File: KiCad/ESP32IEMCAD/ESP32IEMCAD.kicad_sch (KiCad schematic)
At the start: 49 parts, among them J1 AudioJack3, J2 USB_C_Receptacle_PowerOnly_6P, J3 BOOT, J4 UART, J5 JTAG, SW1 SW_Nidec_CAS-120A1, SW2 Interpolation Mode, SW3 Hardware Mute, U1 PCM5102, U2 ESP32-WROOM-32U, U3 MAX97220AETE_T

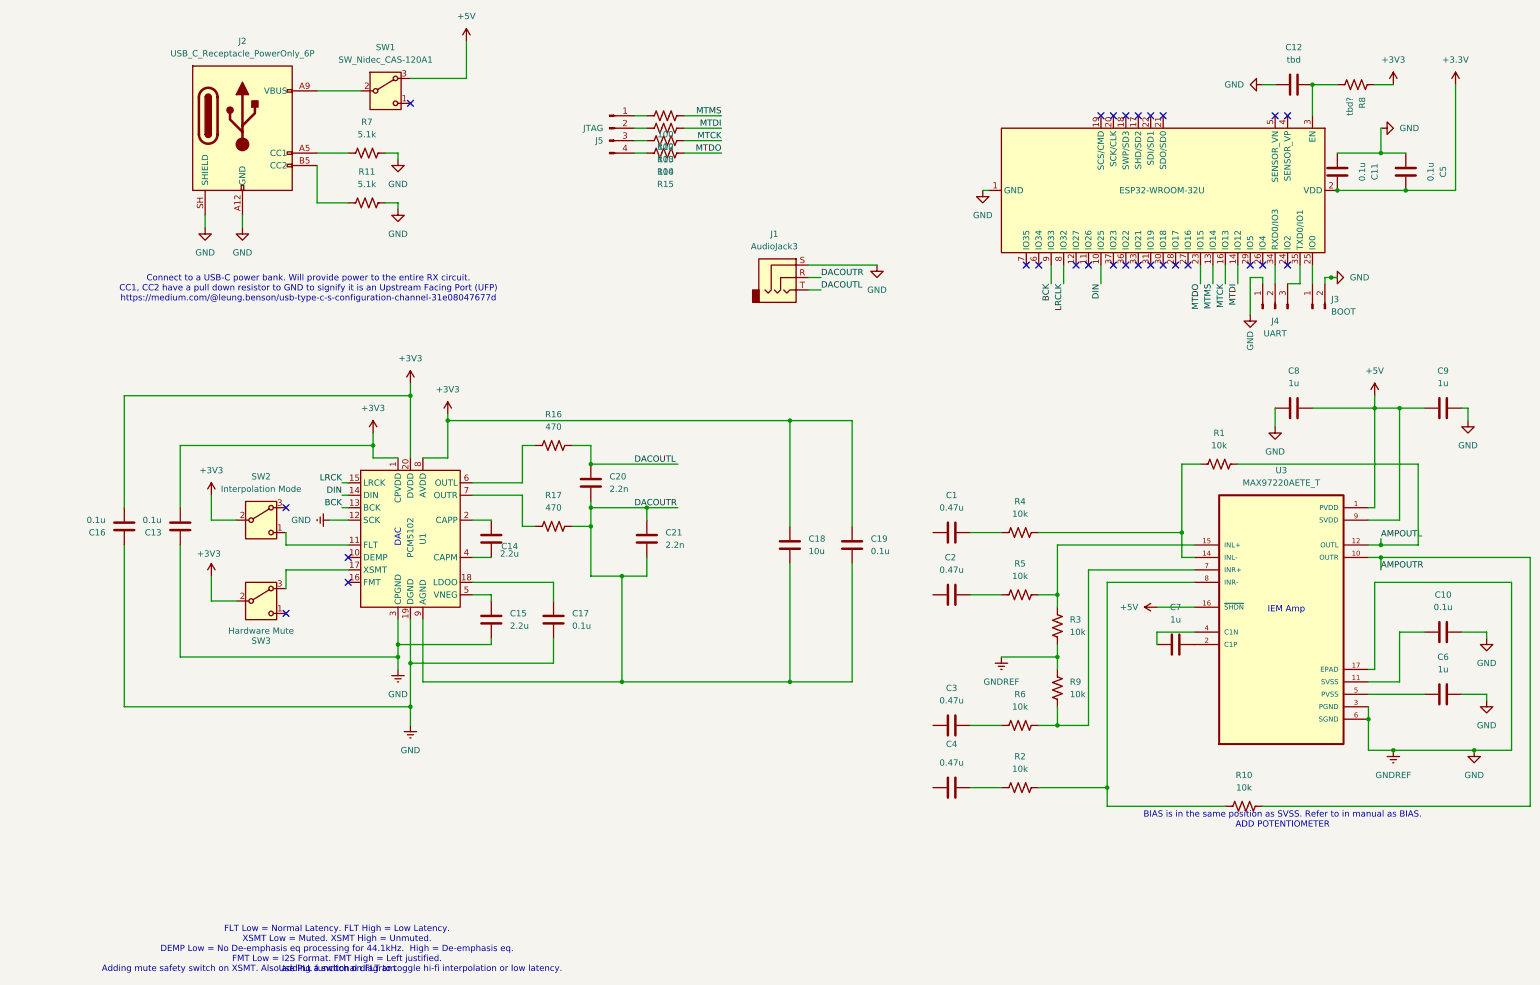
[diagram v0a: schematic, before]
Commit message: First finished schematic for the IEM_RX. Also imported custom symbols.
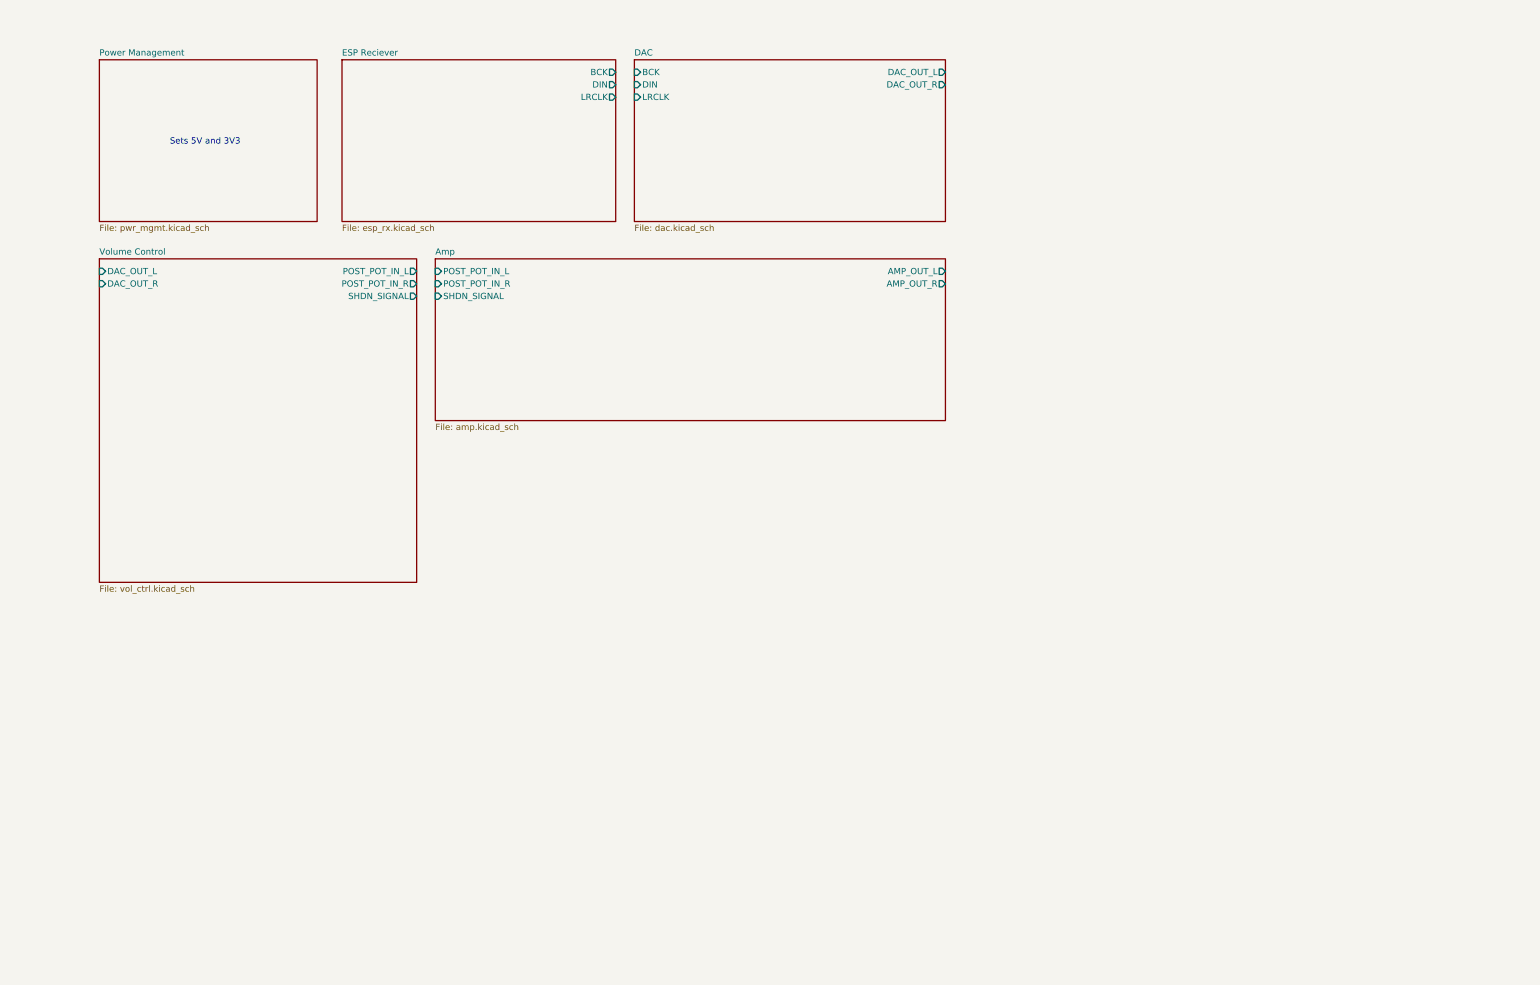
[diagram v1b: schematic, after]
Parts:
- removed C1, C2, C3, C4: 0.47u, symbol Device:C
- removed C10, C11, C13, C16, C17, C19, C5: 0.1u, symbol Device:C
- removed C12: tbd, symbol Device:C
- removed C14, C15: 2.2u, symbol Device:C
- removed C18: 10u, symbol Device:C
- removed C20, C21: 2.2n, symbol Device:C
- removed C6, C7, C8, C9: 1u, symbol Device:C
- removed J1: AudioJack3, symbol Connector_Audio:AudioJack3
- removed J2: USB_C_Receptacle_PowerOnly_6P, symbol Connector:USB_C_Receptacle_PowerOnly_6P
- removed J3: BOOT, symbol Connector:Conn_01x02_Pin
- removed J4: UART, symbol Connector:Conn_01x03_Pin
- removed J5: JTAG, symbol Connector:Conn_01x04_Pin
- removed R1, R10, R2, R3, R4, R5, R6, R9: 10k, symbol Device:R_US
- removed R11, R7: 5.1k, symbol Device:R_US
- removed R12, R13, R14, R15: 100, symbol Device:R_US
- removed R16, R17: 470, symbol Device:R_US
- removed R8: tbd?, symbol Device:R_US
- removed SW1: SW_Nidec_CAS-120A1, Button_Switch_SMD:Nidec_Copal_CAS-120A, symbol Switch:SW_Nidec_CAS-120A1
- removed SW2: Interpolation Mode, Button_Switch_SMD:Nidec_Copal_CAS-120A, symbol Switch:SW_Nidec_CAS-120A1
- removed SW3: Hardware Mute, Button_Switch_SMD:Nidec_Copal_CAS-120A, symbol Switch:SW_Nidec_CAS-120A1
- removed U1: PCM5102, Package_SO:TSSOP-20_4.4x6.5mm_P0.65mm, symbol Audio:PCM5102
- removed U2: ESP32-WROOM-32U, RF_Module:ESP32-WROOM-32U, symbol RF_Module:ESP32-WROOM-32U
- removed U3: MAX97220AETE_T, MAX97220AETE_T:QFN50P300X300X80-17N, symbol MAX97220AETE_T:MAX97220AETE_T
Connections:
- no-connect marks 27 -> 0
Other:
- added sheet Amp (amp.kicad_sch)
- added sheet DAC (dac.kicad_sch)
- added sheet ESP Reciever (esp_rx.kicad_sch)
- added sheet Power Management (pwr_mgmt.kicad_sch)
- added sheet Volume Control (vol_ctrl.kicad_sch)
- note added: "Sets 5V and 3V3"
- note removed: "Adding mute safety switch on XSMT. Also adding a switch on FLT to toggle hi-fi interpolation or low latency."
- note removed: "BIAS is in the same position as SVSS. Refer to in manual as BIAS. ADD POTENTIOMETER"
- note removed: "Connect to a USB-C power bank. Will provide power to the entire RX circuit. CC1, CC2 have a pull down resistor to GND to signify it is an Upstream Facing Port (UFP) https://medium.com/@leung.benson/usb-type-c-s-configuration-channel-31e08047677d"
- note removed: "DAC"
- note removed: "FLT Low = Normal Latency. FLT High = Low Latency. XSMT Low = Muted. XSMT High = Unmuted. DEMP Low = No De-emphasis eq processing for 44.1kHz. High = De-emphasis eq. FMT Low = I2S Format. FMT High = Left justified. Use PLL functional diagram"
- note removed: "IEM Amp"
